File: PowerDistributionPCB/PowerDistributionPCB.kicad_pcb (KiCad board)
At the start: 4 copper layers, 68 parts, among them J1 USB3_A, K1 RT314F05(gen), K2 RT314F05(gen), K3 RT314F05(gen), K4 RT314F05(gen), Q1 AOD4185, Q10 MMBT2222A, Q11 MMBT2222A, Q12 MMBT2222A, Q2 MMBT2222A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

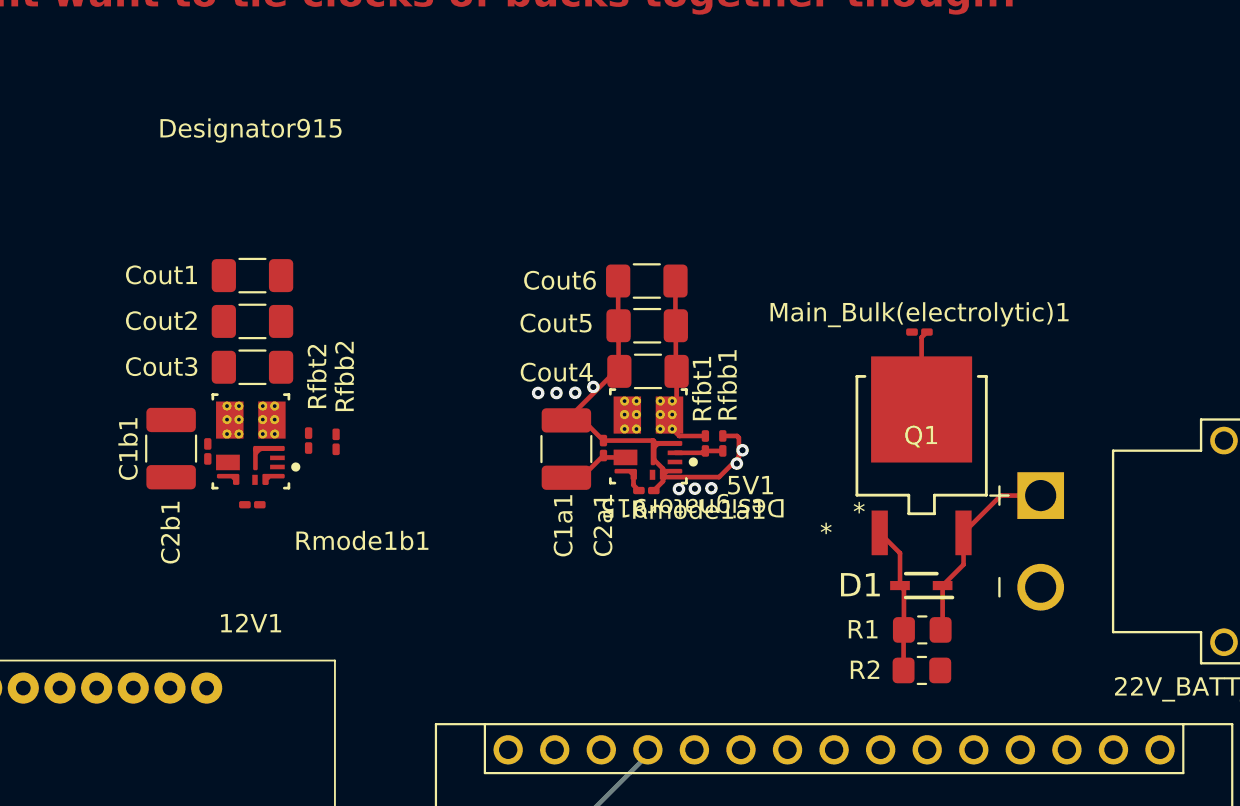
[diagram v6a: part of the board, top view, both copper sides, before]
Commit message: updated buck layout traces
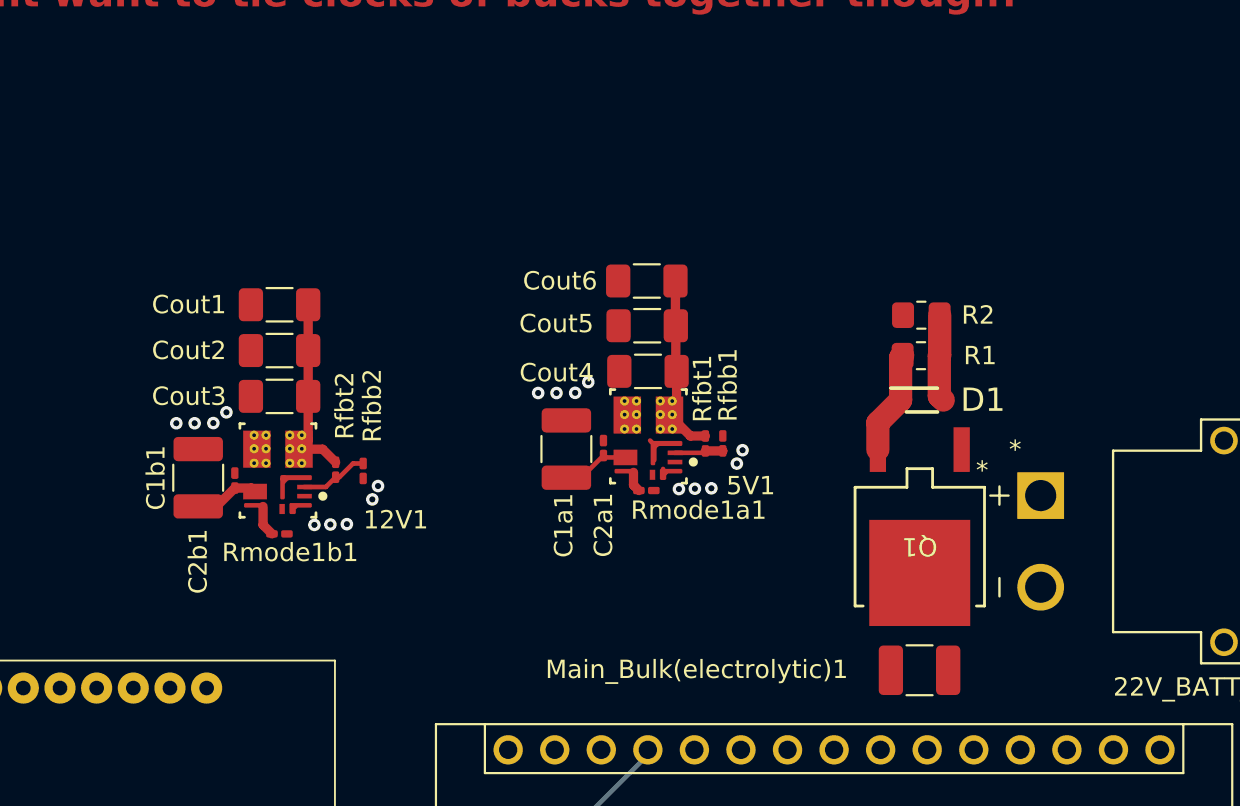
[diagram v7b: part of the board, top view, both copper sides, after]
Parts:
- Main_Bulk(electrolytic)1: footprint Capacitor_SMD:C_0201_0603Metric_Pad0.64x0.40mm_HandSolder -> Capacitor_SMD:C_1210_3225Metric_Pad1.33x2.70mm_HandSolder
- moved R2 19.4 mm to (135.0, 61.2), turned to 0 degrees
- moved Main_Bulk(electrolytic)1 18.5 mm to (134.9, 80.5)
- moved R1 15.0 mm to (135.0, 63.4), turned to 0 degrees
- moved D1 10.1 mm to (135.0, 65.8), turned to 0 degrees
- moved Q1 6.05 mm to (134.9, 73.8), turned to 180 degrees
- moved 12V1 2.17 mm to (99.9, 69.6)
- moved C1b1 2.17 mm to (95.5, 70.0)
- moved C2b1 2.17 mm to (97.5, 70.2)
- moved Cout1 2.17 mm to (100.0, 60.6)
- moved Cout2 2.17 mm to (100.0, 63.1)
- moved Cout3 2.17 mm to (100.0, 65.6)
- moved Rfbb2 2.17 mm to (104.5, 69.7)
- moved Rfbt2 2.17 mm to (103.0, 69.6)
- moved Rmode1b1 2.17 mm to (100.0, 73.1)
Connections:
- 12V1 pad 9: unconnected-(12V1-RT_SYNC-Pad9) -> GND
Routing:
- net GND: track 23.9 -> 2.83 mm, vias 3 -> 0
- net 12VBuck: track 7.62 -> 18.0 mm
- net Batt_Vin: track 10.9 -> 5.68 mm
- net Net-(12V1-FB): track 0.00 -> 3.73 mm
- net Sys_Vin: track 3.77 -> 7.36 mm
- net Net-(Q1-D): track 4.34 -> 0.89 mm
- net Net-(D1-A): track 8.13 -> 4.73 mm
- net Net-(12V1-MODE): track 0.00 -> 1.70 mm
- net (no net): vias 6 -> 18

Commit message: updated buck layout and edge cuts
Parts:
- C2, C3, C4: footprint Capacitor_SMD:C_0201_0603Metric_Pad0.64x0.40mm_HandSolder -> Capacitor_SMD:C_0603_1608Metric_Pad1.08x0.95mm_HandSolder
- moved Cout6 15.3 mm to (118.8, 74.6), turned to 0 degrees
- moved U1 14.9 mm to (82.7, 68.6), turned to 180 degrees
- moved R3a1 13.8 mm to (83.0, 62.7)
- moved Cout1 13.6 mm to (98.6, 74.1), turned to 0 degrees
- moved R3b1 13.1 mm to (79.0, 62.7), turned to 180 degrees
- moved Rmode1b1 11.5 mm to (98.6, 61.6), turned to 180 degrees
- moved Rfbb2 11.4 mm to (94.1, 65.1), turned to 90 degrees
- moved C1 11.4 mm to (82.4, 65.6), turned to 180 degrees
- moved L1 10.9 mm to (76.6, 70.3), turned to 180 degrees
- moved Cout5 10.5 mm to (118.8, 72.1), turned to 0 degrees
- moved Rfbb1 9.78 mm to (114.7, 65.7), turned to -90 degrees
- moved C1b1 9.28 mm to (103.1, 64.7), turned to -90 degrees
- moved Rfbt2 8.70 mm to (95.6, 65.1), turned to 90 degrees
- moved Cout2 8.65 mm to (98.6, 71.6), turned to 0 degrees
- moved C1a1 8.18 mm to (123.2, 65.4), turned to -90 degrees
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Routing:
- net Sys_Vin: track 7.36 -> 88.2 mm
- net 3.3VBuck: track 7.62 -> 31.0 mm
- net Net-(U1-EN): track 0.00 -> 16.4 mm, vias 0 -> 2
- net Batt_Vin: track 5.68 -> 15.6 mm
- net Net-(U1-SW): track 0.00 -> 8.22 mm
- net Net-(Q1-D): track 0.89 -> 6.84 mm
- net Net-(D1-A): track 4.73 -> 7.84 mm
- net GND: track 2.83 -> 5.63 mm, vias 0 -> 6
- net Net-(U1-BST): track 0.00 -> 2.67 mm
- added copper zone on F.Cu, net GND
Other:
- board outline added: 89.8 x 107.2 mm
